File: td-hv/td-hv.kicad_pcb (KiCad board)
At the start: 2 copper layers, 90 x 71 mm, 56 parts, among them J1 Conn_01x14, Q1 BSZ42DN25NS3GATMA1, Q12 G3R450MT17J, Q2 BSZ42DN25NS3GATMA1, U1 74HC00, U13 MCP1416, U2 LM2903, U4 2ED2101S06FXUMA1, U7 MIC5504-3.3YM5

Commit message: do some basic fixes
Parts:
- TP10, TP4, TP6, TP7, TP8, TP9: footprint TestPoint:TestPoint_Keystone_5019_Minature -> TestPoint:TestPoint_Keystone_5019_Miniature
- U7: value MIC5504-3.3YM5 -> AP2205
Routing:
- net Net-(R5-Pad2): track 3.64 -> 2.81 mm
- net /flyback/eht out: vias 9 -> 8
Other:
- board text added: "HV Protect"
- board text added: "td-hv v2.1 CERN OHL-W 2023 https://github.com/tdaede/td-crt"
- board text removed: "X-Ray Protect"
- board text removed: "td-hv v2.0 CERN OHL-W 2023 https://github.com/tdaede/td-crt"

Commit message: finish board
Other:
- board text added: "td-hv v2.2 CERN OHL-W 2025 https://github.com/tdaede/td-crt"
- board text removed: "td-hv v2.1 CERN OHL-W 2023 https://github.com/tdaede/td-crt"
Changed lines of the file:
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@@
 		)
 	)
-	(gr_text "td-hv v2.1 CERN OHL-W 2023\nhttps://github.com/tdaede/td-crt"
+	(gr_text "td-hv v2.2 CERN OHL-W 2025\nhttps://github.com/tdaede/td-crt"
 		(at 117 135 0)
 		(layer "F.SilkS")

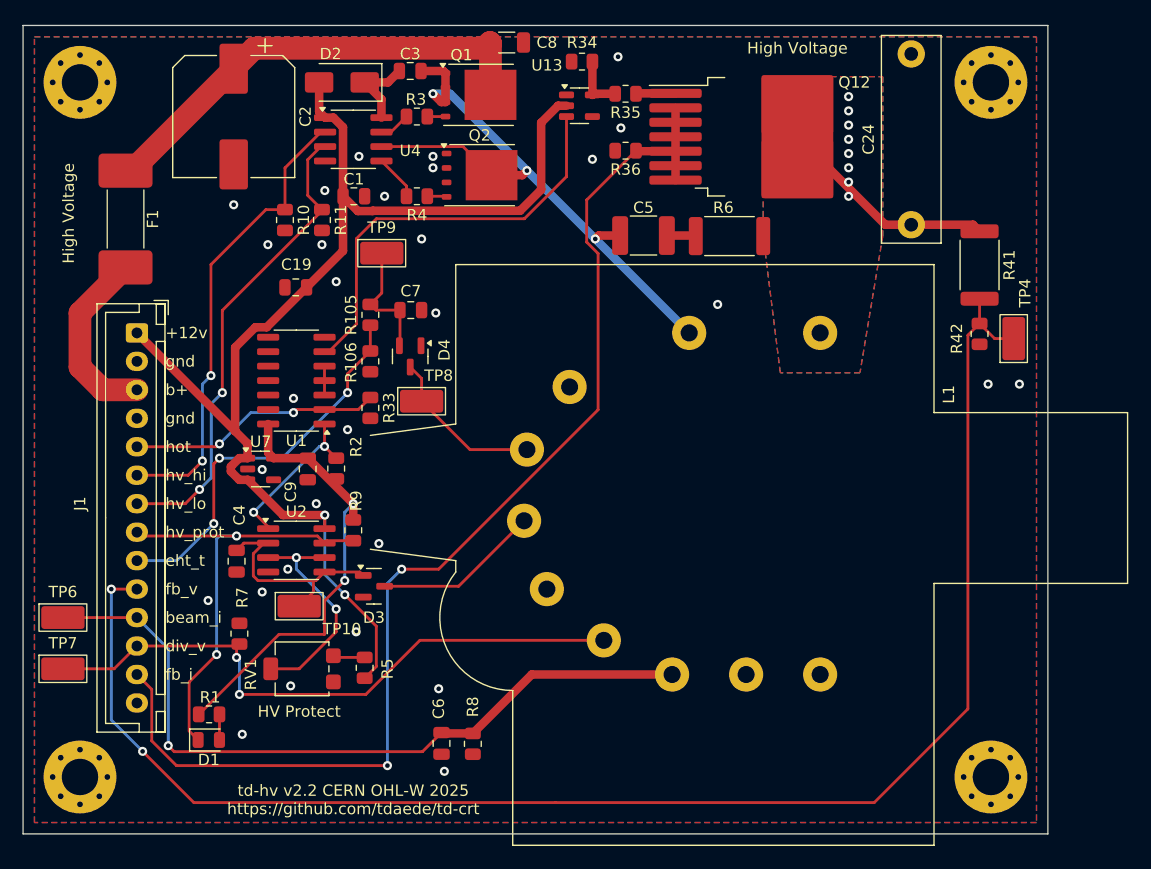
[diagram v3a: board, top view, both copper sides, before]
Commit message: Adjust td-hv pin spacing and add a bypass jumper
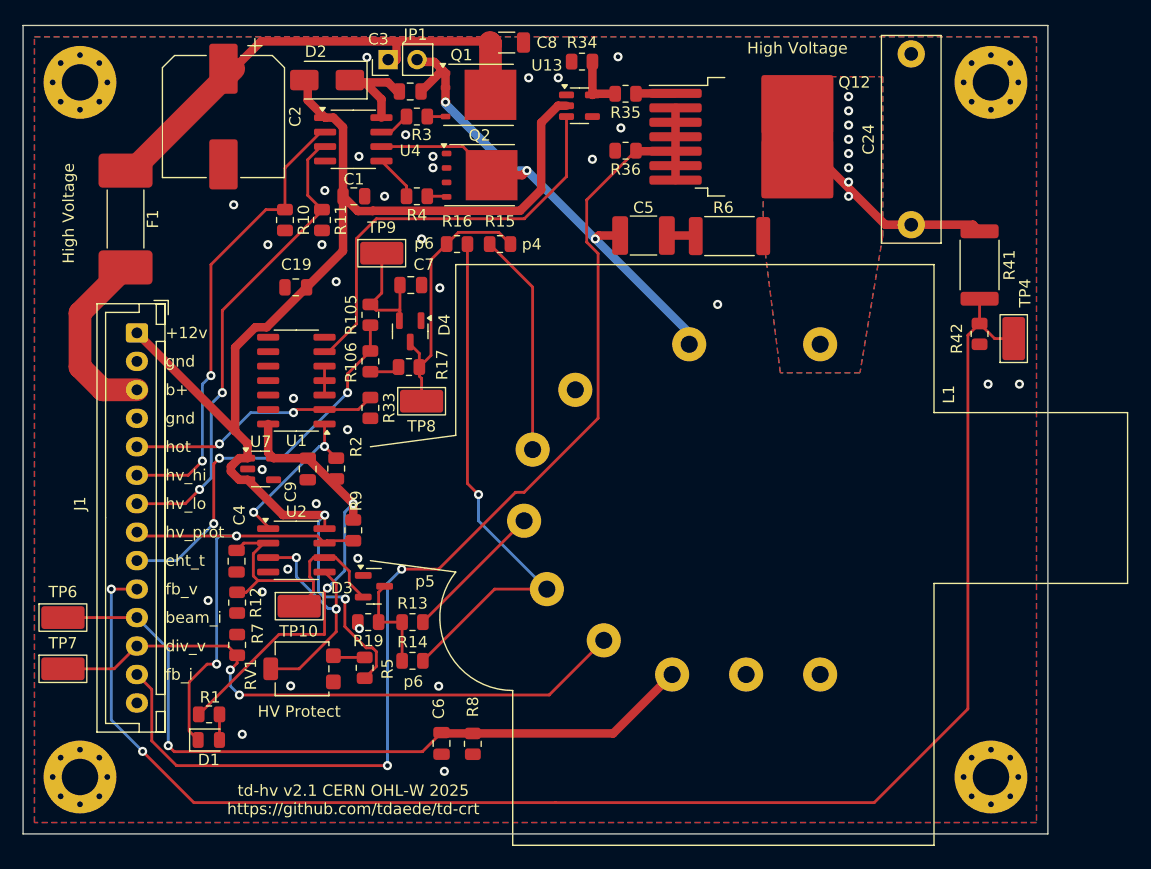
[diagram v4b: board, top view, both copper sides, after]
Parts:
- added JP1: Jumper_2_Open, Connector_PinHeader_2.54mm:PinHeader_1x02_P2.54mm_Vertical, F.Cu at (120.1, 70.0)
- added R12: 1k, Resistor_SMD:R_0805_2012Metric, F.Cu at (106.8, 117.7)
- added R13: 10k, Resistor_SMD:R_0805_2012Metric, F.Cu at (122.2, 119.4)
- added R14: 1k, Resistor_SMD:R_0805_2012Metric, F.Cu at (122.2, 122.8)
- added R15: 1k, Resistor_SMD:R_0805_2012Metric, F.Cu at (129.9, 86.2)
- added R16: 1k, Resistor_SMD:R_0805_2012Metric, F.Cu at (126.1, 86.2)
- added R17: 1k, Resistor_SMD:R_0805_2012Metric, F.Cu at (121.9, 97.0)
- added R19: 1k, Resistor_SMD:R_0805_2012Metric, F.Cu at (118.3, 119.4)
- moved C7 2.20 mm to (122.0, 89.8)
- moved D4 2.20 mm to (122.0, 93.9)
- moved C3 1.80 mm to (122.0, 72.8)
- moved D2 1.32 mm to (114.7, 71.8)
- moved R7 1.01 mm to (106.8, 121.4)
- moved C2 0.90 mm to (105.6, 75.0)
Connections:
- D3 pad 1: Net-(U2A--) -> unconnected-(D3-Pad1)
- D3 pad 2: unconnected-(D3-Pad2) -> Net-(U2A--)
- L1 pad 4: Net-(D4-Pad3) -> Net-(L1-Pad4)
- L1 pad 5: Net-(D3-Pad3) -> Net-(L1-Pad5)
- L1 pad 6: unconnected-(L1-Pad6) -> Net-(L1-Pad6)
- U2 pad 5: Net-(U2A--) -> Net-(U2A-+)
- U2 pad 6: Net-(U2A-+) -> Net-(U2A--)
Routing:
- net Net-(L1-Pad6): track 0.00 -> 46.7 mm, vias 0 -> 1
- net Net-(L1-Pad4): track 0.00 -> 19.6 mm
- net Net-(L1-Pad5): track 0.00 -> 12.6 mm
- net Net-(D4-Pad3): track 14.4 -> 23.9 mm
- net Net-(U2A--): track 19.7 -> 25.9 mm
- net Net-(D3-Pad3): track 14.6 -> 8.83 mm
- net GND: track 0.00 -> 2.65 mm, vias 30 -> 34
- net +12V: track 108.8 -> 111.3 mm
- net HT: track 41.3 -> 43.2 mm
- net Net-(U2A-+): track 20.0 -> 21.6 mm
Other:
- board text added: "p4"
- board text added: "p5"
- board text added: "p6"
- board text added: "td-hv v2.1 CERN OHL-W 2025 https://github.com/tdaede/td-crt"
- board text removed: "td-hv v2.2 CERN OHL-W 2025 https://github.com/tdaede/td-crt"
